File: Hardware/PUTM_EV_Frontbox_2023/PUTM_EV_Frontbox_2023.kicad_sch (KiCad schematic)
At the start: 29 parts, among them J2 Conn_01x04, J5 Conn_02x14_Counter_Clockwise, SW1 Reset switch, U1 STM32G473RCTx

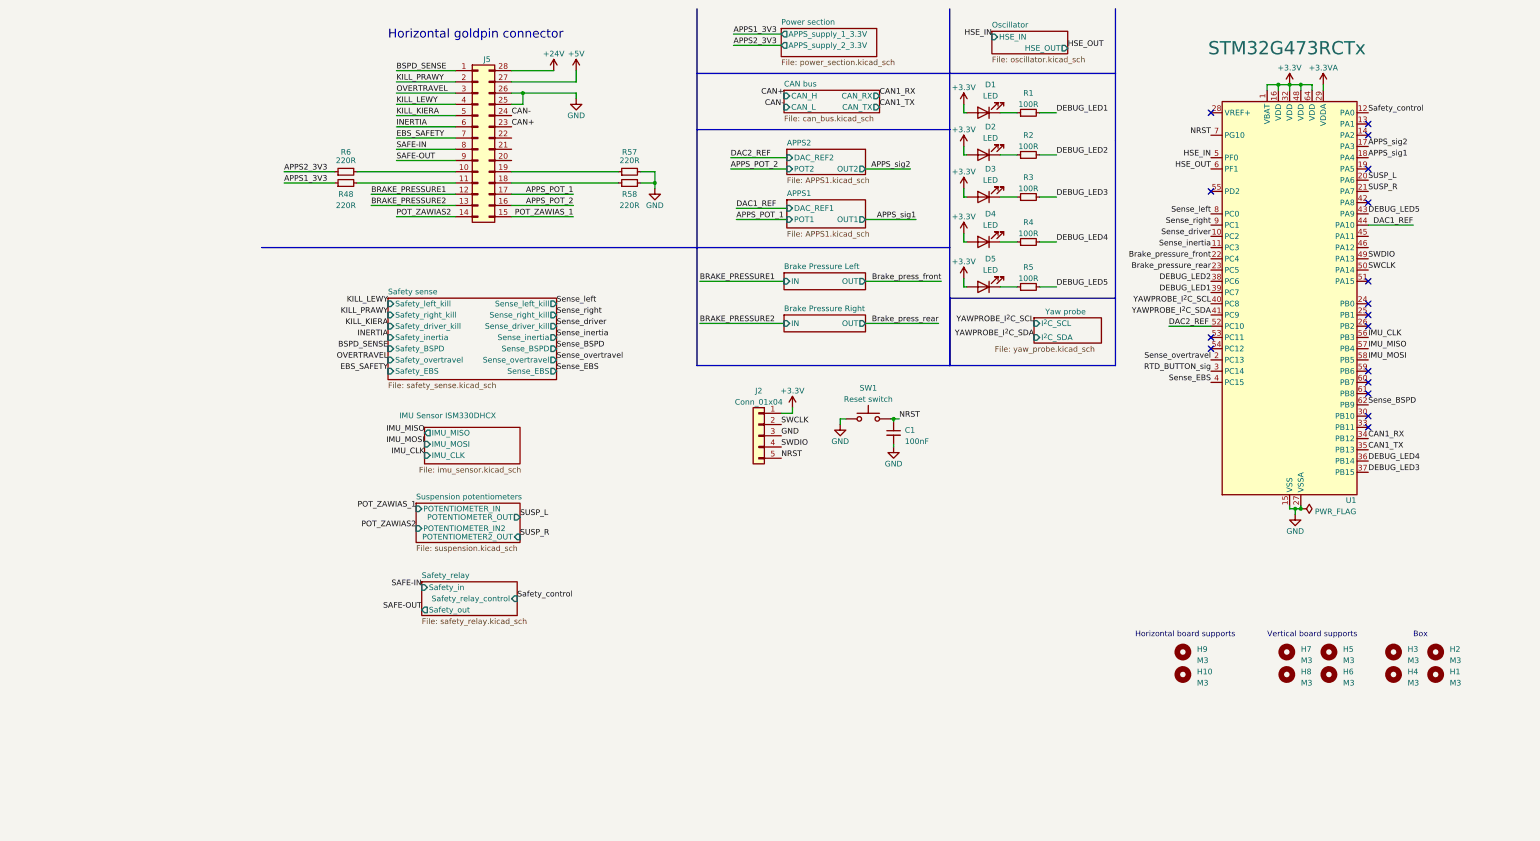
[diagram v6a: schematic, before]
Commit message: Added additional analog measurement ciructry
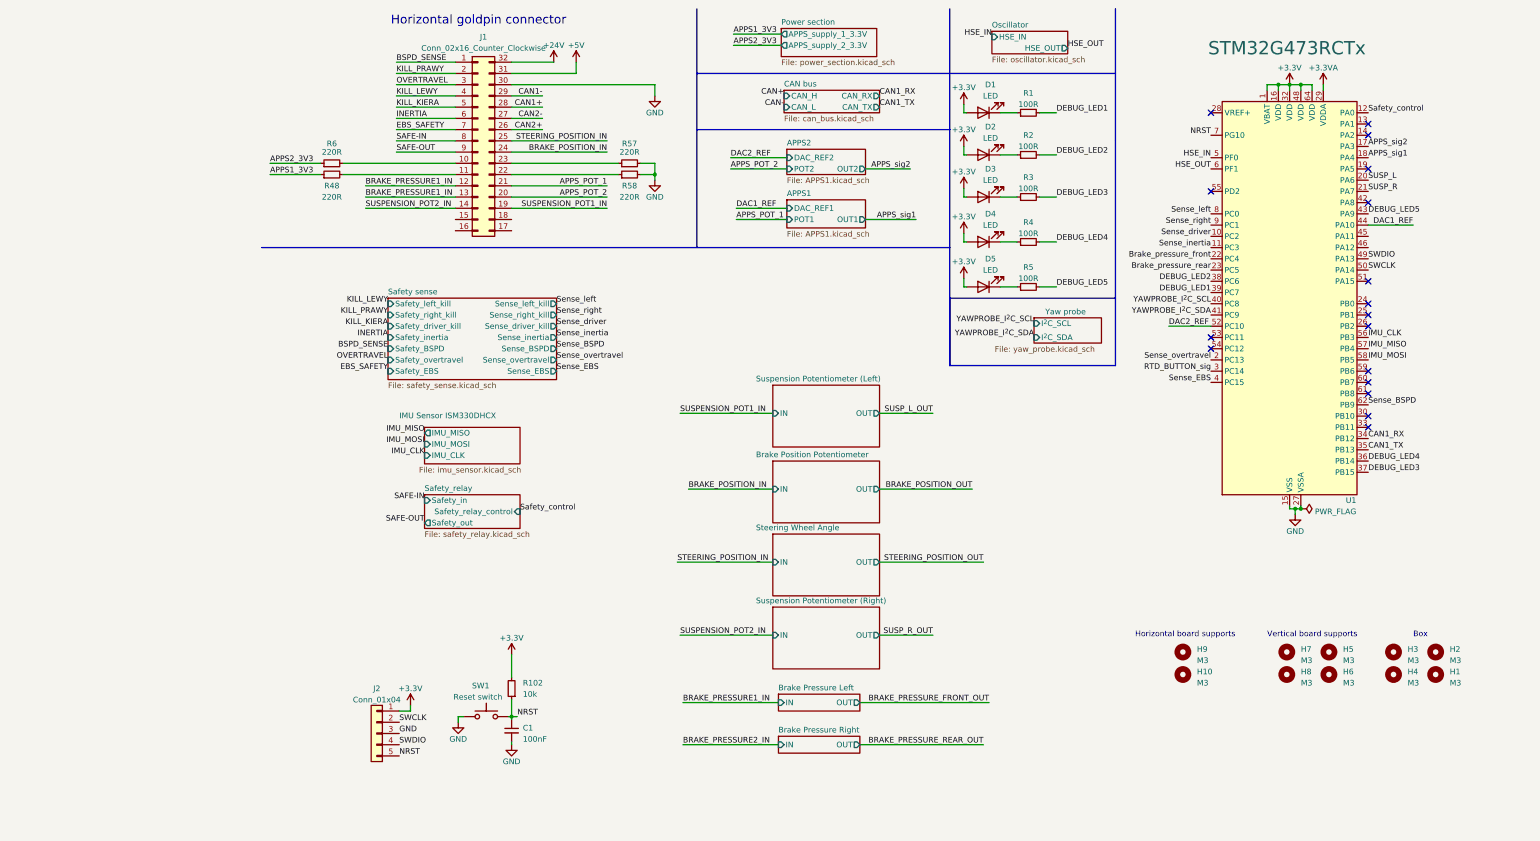
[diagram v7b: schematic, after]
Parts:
- removed J5: Conn_02x14_Counter_Clockwise, Connector_PinSocket_2.54mm:PinSocket_2x14_P2.54mm_Vertical, symbol Connector_Generic:Conn_02x14_Counter_Clockwise
- added J1: Conn_02x16_Counter_Clockwise, symbol Connector_Generic:Conn_02x16_Counter_Clockwise
- added R102: 10k, Resistor_SMD:R_0402_1005Metric, symbol Device:R_Small
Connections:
- net +24V: now also J1.32 (Pin_32)
- net +3.3V: now also R102.2
- net +5V: now also J1.31 (Pin_31)
- net APPS_POT_1: now also J1.21 (Pin_21)
- net APPS_POT_2: now also J1.20 (Pin_20)
- net BSPD_SENSE: now also J1.1 (Pin_1)
- net EBS_SAFETY: now also J1.7 (Pin_7)
- net GND: now also J1.30 (Pin_30)
- net INERTIA: now also J1.6 (Pin_6)
- net KILL_KIERA: now also J1.5 (Pin_5)
- net KILL_LEWY: now also J1.4 (Pin_4)
- net KILL_PRAWY: now also J1.2 (Pin_2)
- net NRST: now also R102.1
- net OVERTRAVEL: now also J1.3 (Pin_3)
- net SAFE-IN: now also J1.8 (Pin_8)
- net SAFE-OUT: now also J1.9 (Pin_9)
- net at R48.2: now also J1.11 (Pin_11)
- net at R6.2: now also J1.10 (Pin_10)
- net at R58.1: now also J1.22 (Pin_22)
- net at R57.1: now also J1.23 (Pin_23)
- new net BRAKE_POSITION_IN: J1.24 (Pin_24)
- new net BRAKE_PRESSURE1_IN: J1.12 (Pin_12), J1.13 (Pin_13)
- new net CAN1+: J1.28 (Pin_28)
- new net CAN1-: J1.29 (Pin_29)
- new net CAN2+: J1.26 (Pin_26)
- new net CAN2-: J1.27 (Pin_27)
- new net STEERING_POSITION_IN: J1.25 (Pin_25)
- new net SUSPENSION_POT1_IN: J1.19 (Pin_19)
- new net SUSPENSION_POT2_IN: J1.14 (Pin_14)
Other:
- removed sheet Suspension potentiometers
- added sheet Brake Position Potentiometer (suspension_potentiometer.kicad_sch)
- added sheet Steering Wheel Angle (suspension_potentiometer.kicad_sch)
- added sheet Suspension Potentiometer (Left) (suspension_potentiometer.kicad_sch)
- added sheet Suspension Potentiometer (Right) (suspension_potentiometer.kicad_sch)
- moved on the sheet: C1, J2, R48, R57, R58, R6, SW1

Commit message: Schematic updates
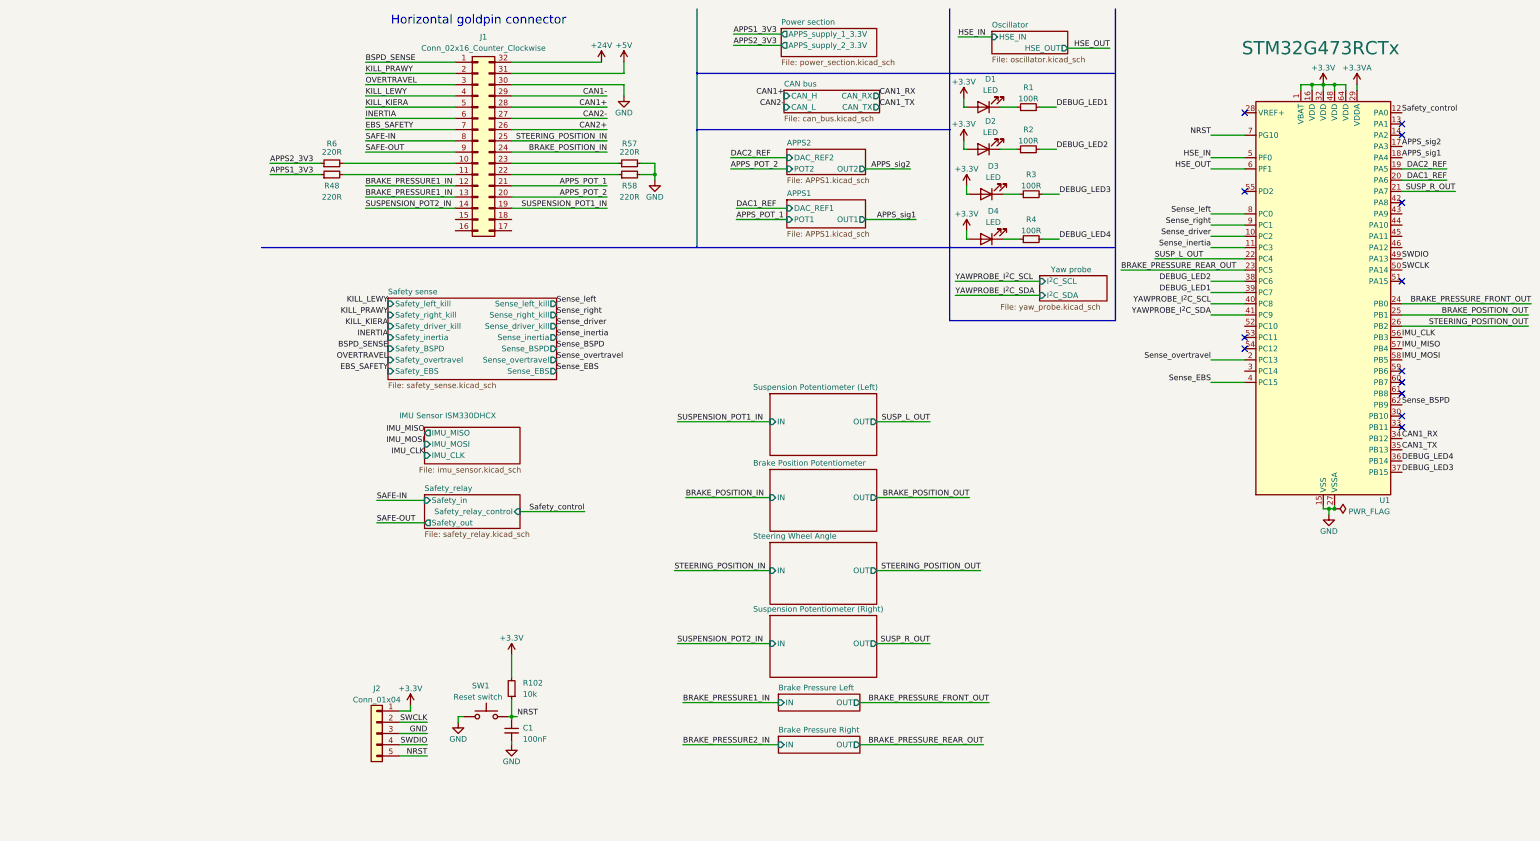
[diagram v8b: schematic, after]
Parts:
- removed D5: LED, LED_SMD:LED_0201_0603Metric, symbol Device:LED
- removed H1, H10, H2, H3, H4, H5, H6, H7, H8, H9: M3, MountingHole:MountingHole_2mm, symbol Mechanical:MountingHole
- removed R5: 100R, Resistor_SMD:R_0402_1005Metric, symbol Device:R_Small
- D1, D2, D3, D4: footprint LED_SMD:LED_0201_0603Metric -> LED_SMD:LED_0603_1608Metric_Pad1.05x0.95mm_HandSolder
- R1, R102, R2, R3, R4: footprint Resistor_SMD:R_0402_1005Metric -> Resistor_SMD:R_0603_1608Metric_Pad0.98x0.95mm_HandSolder
- R48, R57, R58, R6: footprint (none) -> Resistor_SMD:R_0603_1608Metric_Pad0.98x0.95mm_HandSolder
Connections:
- net Brake_pressure_front is gone; now on net SUSP_L_OUT: U1.22 (PC4)
- net Brake_pressure_rear is gone; now on net BRAKE_PRESSURE_REAR_OUT: U1.23 (PC5)
- net SUSP_L is gone; now on net DAC1_REF: U1.20 (PA6)
- net SUSP_R is gone; now on net SUSP_R_OUT: U1.21 (PA7)
- net BRAKE_POSITION_OUT: now also U1.25 (PB1)
- net BRAKE_PRESSURE_FRONT_OUT: now also U1.24 (PB0)
- net DAC1_REF: no longer U1.44 (PA10)
- net DAC2_REF: now also U1.19 (PA5); no longer U1.52 (PC10)
- net STEERING_POSITION_OUT: now also U1.26 (PB2)
- net DEBUG_LED5: no longer names the net of U1.43 (PA9)
- net RTD_BUTTON_sig: no longer names the net of U1.3 (PC14)
- no-connect marks 17 -> 13
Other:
- note removed: "Box"
- note removed: "Horizontal board supports"
- note removed: "Vertical board supports"
- moved on the sheet: D1, D2, D3, D4, R1, R2, R3, R4, U1
